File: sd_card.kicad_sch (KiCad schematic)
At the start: 19 parts, among them J5 Screw_Terminal_01x03, J702 DM3AT-SF-PEJM5_40_, U11 EMIF06-MSD02N16, U701 ADM2565EBRNZ

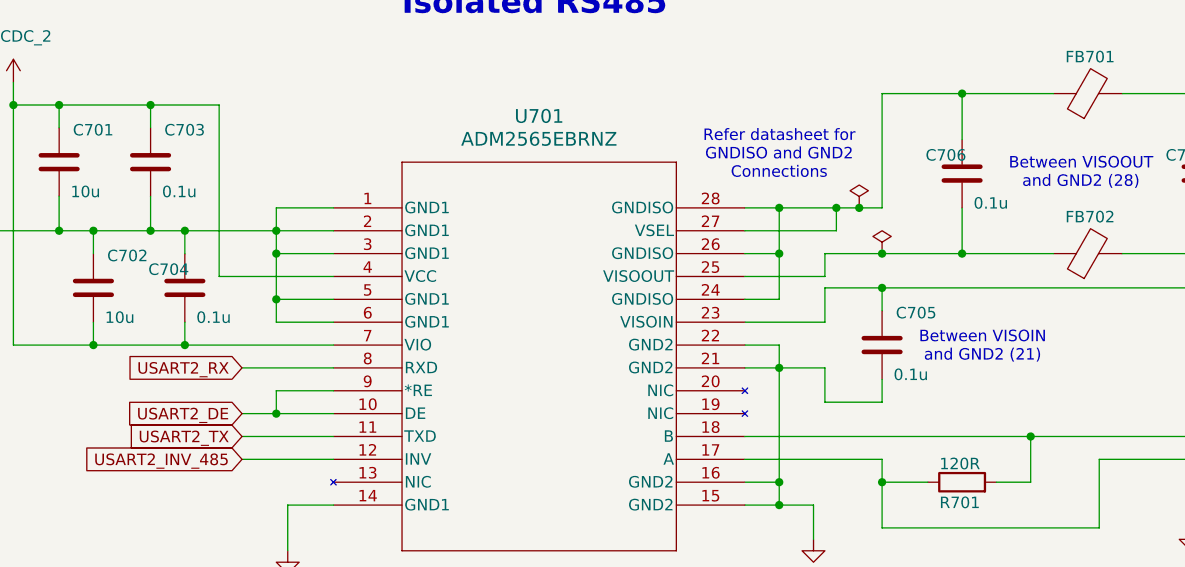
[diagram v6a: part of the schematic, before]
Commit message: schematics errors fixed and ready for PCB
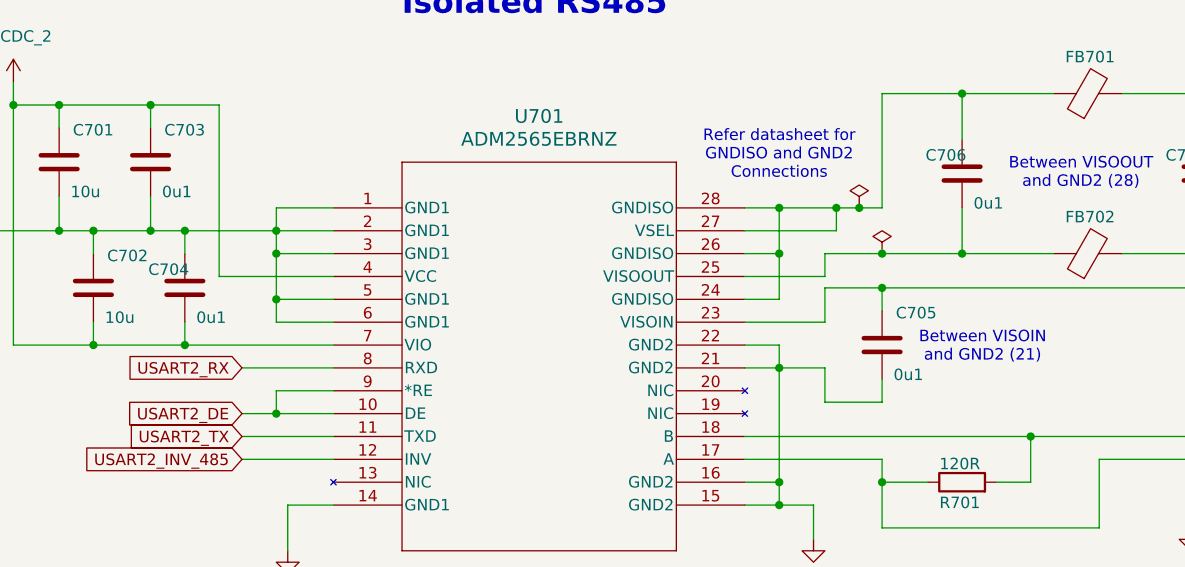
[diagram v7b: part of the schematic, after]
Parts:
- C703, C704, C705, C706: value 0.1u -> 0u1
- TP701, TP702, TP703: Distributor_Link https://www.mouser.com/ProductDetail/Keystone-Electronics/5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 -> (none); Manufacturer_Name Keystone Electronics -> (none); Manufacturer_Part_Number 5000 -> (none)
- U11: footprint EMS:EMIF06-MSD02N16 -> AMS-CM:EMIF06-MSD02N16; symbol AMS-CM:EMIF06-MSD02N16 -> EMS:EMIF06-MSD02N16
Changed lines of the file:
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@@
 	)
 	(symbol
-		(lib_id "AMS-CM:EMIF06-MSD02N16")
+		(lib_id "EMS:EMIF06-MSD02N16")
 		(at 181.61 40.64 0)
 		(unit 1)
@@
 			)
 		)
-		(property "Footprint" "EMS:EMIF06-MSD02N16"
+		(property "Footprint" "AMS-CM:EMIF06-MSD02N16"
 			(at 218.44 135.56 0)
 			(effects
@@
 			)
 		)
-		(property "Value" "0.1u"
+		(property "Value" "0u1"
 			(at 38.1 112.522 0)
 			(effects
@@
 			)
 		)
-		(property "Datasheet" "https://www.mouser.com/datasheet/2/215/000-5004-741320.pdf"
+		(property "Datasheet" "~"
 			(at 46.99 184.15 0)
 			(effects
@@
 			)
 		)
-		(property "Distributor_Link" "https://www.mouser.com/ProductDetail/Keystone-Electronics/5000?qs=q0tsjPZWdm%252B9SiiTAbEwUw%3D%3D"
+		(property "Distributor_Link" "~"
 			(at 46.99 189.23 0)
 			(effects
@@
 			)
 		)
-		(property "Manufacturer_Name" "Keystone Electronics"
+		(property "Manufacturer_Name" "~"
 			(at 46.99 189.23 0)
 			(effects
@@
 			)
 		)
-		(property "Manufacturer_Part_Number" "5000"
+		(property "Manufacturer_Part_Number" "~"
 			(at 46.99 189.23 0)
 			(effects
@@
 			)
 		)
-		(property "Value" "0.1u"
+		(property "Value" "0u1"
 			(at 41.91 126.492 0)
 			(effects
@@
 			)
 		)
-		(property "Datasheet" "https://www.mouser.com/datasheet/2/215/000-5004-741320.pdf"
+		(property "Datasheet" "~"
 			(at 25.4 184.15 0)
 			(effects
@@
 			)
 		)
-		(property "Distributor_Link" "https://www.mouser.com/ProductDetail/Keystone-Electronics/5000?qs=q0tsjPZWdm%252B9SiiTAbEwUw%3D%3D"
+		(property "Distributor_Link" "~"
 			(at 25.4 189.23 0)
 			(effects
@@
 			)
 		)
-		(property "Manufacturer_Name" "Keystone Electronics"
+		(property "Manufacturer_Name" "~"
 			(at 25.4 189.23 0)
 			(effects
@@
 			)
 		)
-		(property "Manufacturer_Part_Number" "5000"
+		(property "Manufacturer_Part_Number" "~"
 			(at 25.4 189.23 0)
 			(effects
@@
 			)
 		)
-		(property "Value" "0.1u"
+		(property "Value" "0u1"
 			(at 119.38 132.842 0)
 			(effects
@@
 			)
 		)
-		(property "Datasheet" "https://www.mouser.com/datasheet/2/215/000-5004-741320.pdf"
+		(property "Datasheet" "~"
 			(at 69.85 184.15 0)
 			(effects
@@
 			)
 		)
-		(property "Distributor_Link" "https://www.mouser.com/ProductDetail/Keystone-Electronics/5000?qs=q0tsjPZWdm%252B9SiiTAbEwUw%3D%3D"
+		(property "Distributor_Link" "~"
 			(at 69.85 189.23 0)
 			(effects
@@
 			)
 		)
-		(property "Manufacturer_Name" "Keystone Electronics"
+		(property "Manufacturer_Name" "~"
 			(at 69.85 189.23 0)
 			(effects
@@
 			)
 		)
-		(property "Manufacturer_Part_Number" "5000"
+		(property "Manufacturer_Part_Number" "~"
 			(at 69.85 189.23 0)
 			(effects
@@
 			)
 		)
-		(property "Value" "0.1u"
+		(property "Value" "0u1"
 			(at 128.27 113.792 0)
 			(effects

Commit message: new version created. Now at v2.0.0
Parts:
- U11: footprint AMS-CM:EMIF06-MSD02N16 -> EMS:EMIF06-MSD02N16
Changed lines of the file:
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@@
 			)
 		)
-		(property "Footprint" "AMS-CM:EMIF06-MSD02N16"
+		(property "Footprint" "EMS:EMIF06-MSD02N16"
 			(at 218.44 135.56 0)
 			(effects
